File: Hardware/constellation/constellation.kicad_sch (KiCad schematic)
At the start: 0 parts

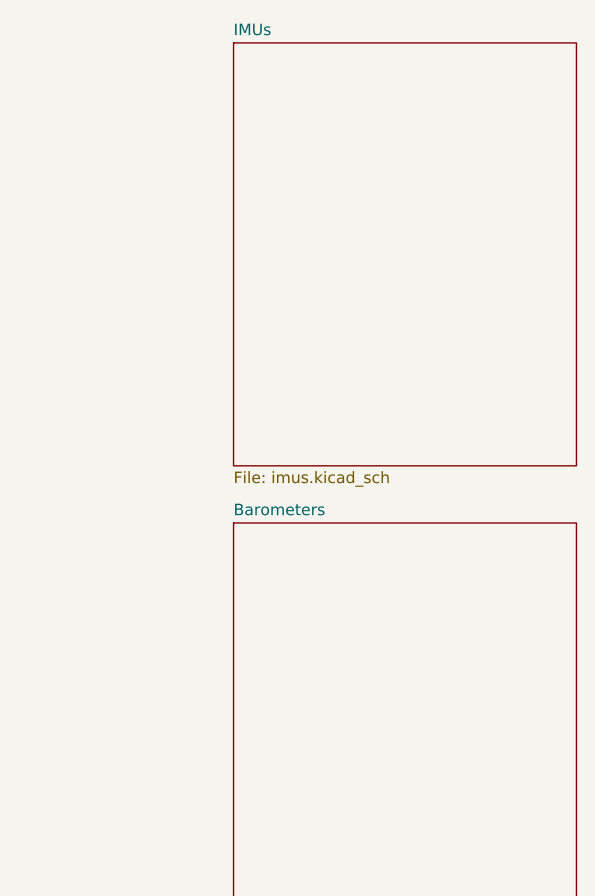
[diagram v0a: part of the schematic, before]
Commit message: add the hierarchal pins to the imu block
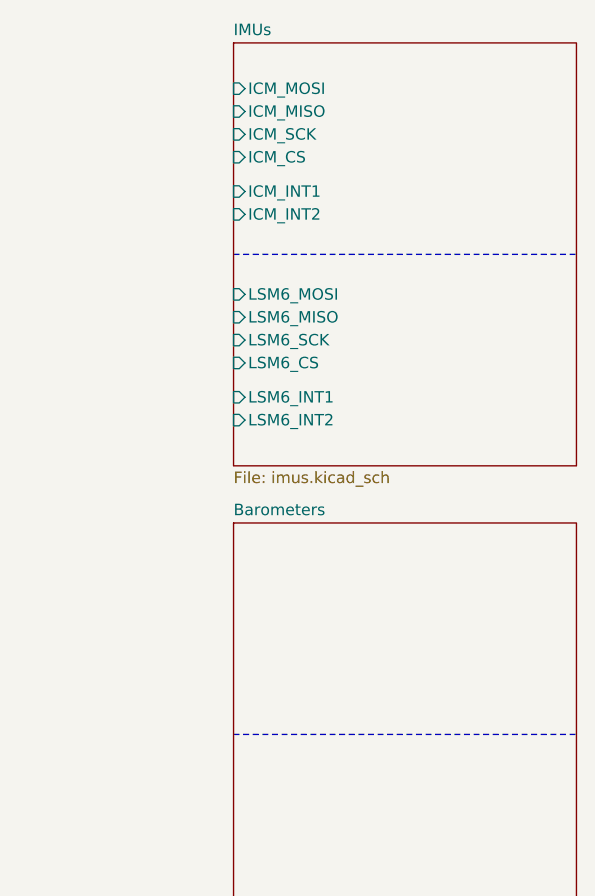
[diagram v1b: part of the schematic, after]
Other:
- sheet IMUs ports: added ICM_CS, ICM_INT1, ICM_INT2, ICM_MISO, ICM_MOSI, ICM_SCK, LSM6_CS, LSM6_INT1, LSM6_INT2, LSM6_MISO, LSM6_MOSI, LSM6_SCK; removed none

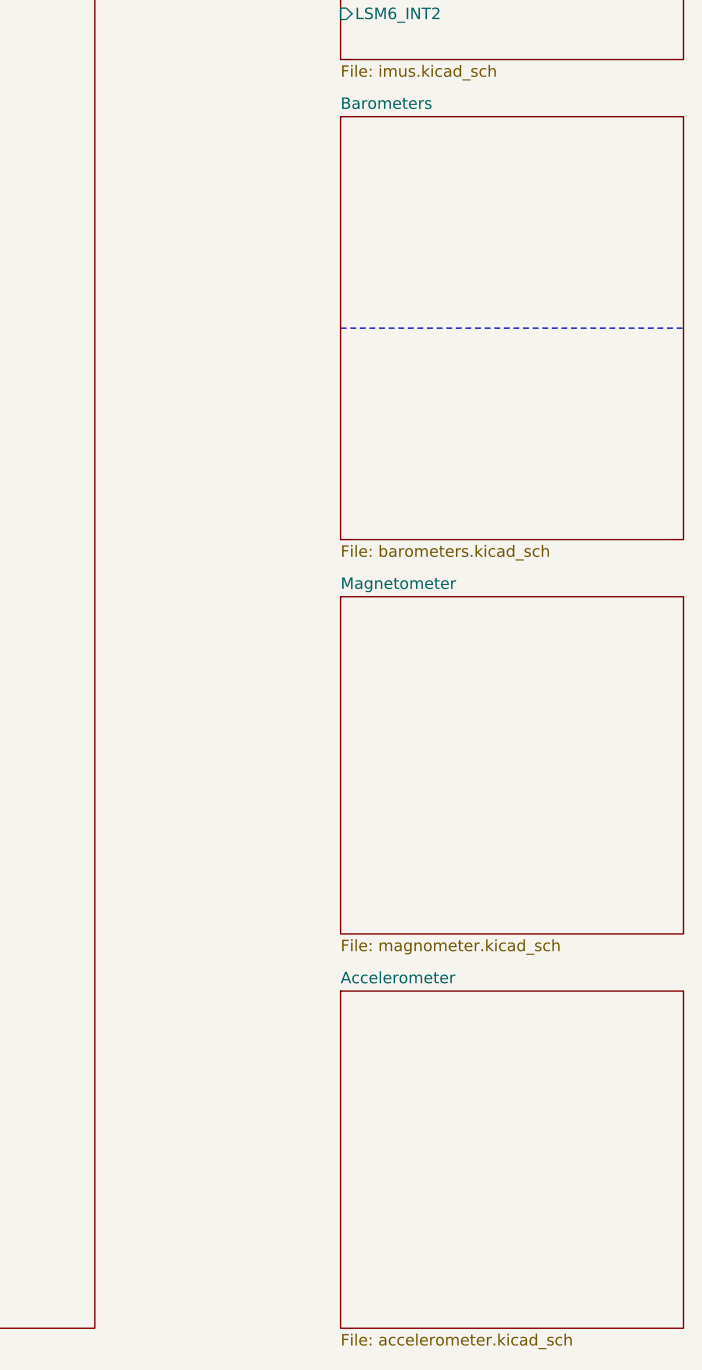
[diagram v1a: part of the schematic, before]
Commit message: add gnss short detection and lna_en supervisor
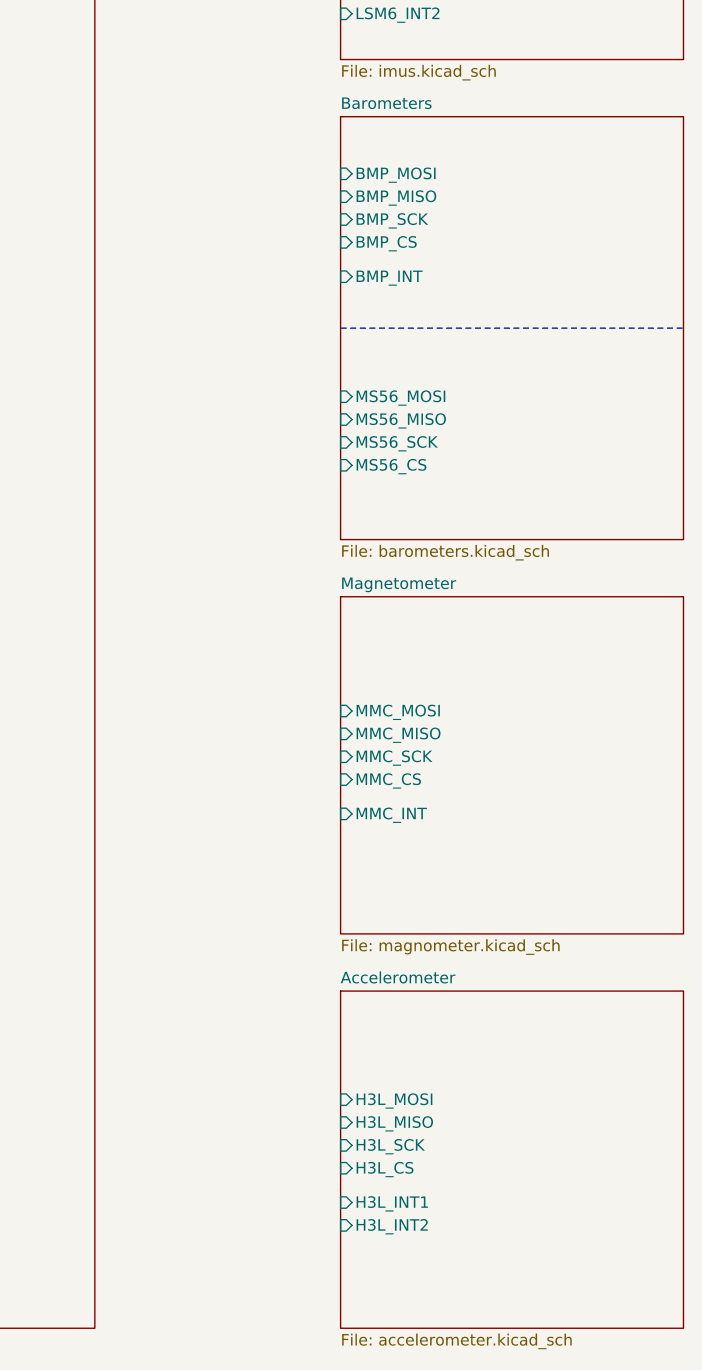
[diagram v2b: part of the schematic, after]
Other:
- sheet Accelerometer ports: added H3L_CS, H3L_INT1, H3L_INT2, H3L_MISO, H3L_MOSI, H3L_SCK; removed none
- sheet Barometers ports: added BMP_CS, BMP_INT, BMP_MISO, BMP_MOSI, BMP_SCK, MS56_CS, MS56_MISO, MS56_MOSI, MS56_SCK; removed none
- sheet Magnetometer ports: added MMC_CS, MMC_INT, MMC_MISO, MMC_MOSI, MMC_SCK; removed none

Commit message: convert gnss into hierarchal
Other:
- added sheet GNSS (gnss.kicad_sch)
